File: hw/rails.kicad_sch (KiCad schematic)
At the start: 20 parts, among them U201 LM5164, U202 TLV76733

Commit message: Choose the buck inductor; record three design items the parts exposed
L201: Wurth 7447714330 (WE-PD 1050, 33 uH, Isat 2.9 A typ, AEC-Q200
Grade 1) -- 1.72x the 1.18 A worst peak after a -30% hot derate,
closing the Isat gap buck_preregulator.cir left open. Land pattern is
not in KiCad 7; phase 3.

Three items that are not part choices, each pinned as a check:
- POWER-PATH: injector and EGR current flows through pin 21, the EMI
  filter and a reverse FET sized for 5 A; pins 04/06 are 10 A battery
  feeds used only as senses. L101/L102/F101 wait on the decision.
- BOOST-SLOPE: by TI SLVS861F Eq. 9 the drawn 82 mOhm sense resistor
  exceeds the subharmonic ceiling at cranking (44.9 mOhm), and the
  330 uH it needs does not exist at a 2.2 A saturation rating.
- SENSOR-PTC: real PTCs are specified 0.40-5.00 ohm, not "3.0 ohm
  +/-30%", and Ihold halves at 85 C.

The netlist gate now counts the power ground as an open item: GND
reaches the connector only through sensor-ground pins. Removes a stale
EGR note from the connector sheet.

24/24 sim blocks, netlist gate passing with 2 named open items.
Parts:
- L201: value 33uH -> 7447714330; Chosen (none) -> Wurth WE-PD 1050, 33 uH, Isat 2.9 A typ, IR 2.5 A, 79 mOhm 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; Class (none) -> 33uH; MPN (none) -> 7447714330
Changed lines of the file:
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@@
       (effects (font (size 1.27 1.27)))
     )
-    (property "Value" "33uH" (id 1) (at 284.0 90.08 0)
+    (property "Value" "7447714330" (id 1) (at 284.0 90.08 0)
       (effects (font (size 1.27 1.27)))
     )
@@
       (effects (font (size 1.27 1.27)) hide)
     )
-    (property "Source" "buck_preregulator.cir L1 -- sized by ripple at the 40 V worst case, not at nominal" (id 4) (at 284.0 85.0 0)
+    (property "MPN" "7447714330" (id 4) (at 284.0 85.0 0)
       (effects (font (size 1.27 1.27)) hide)
     )
+    (property "Class" "33uH" (id 5) (at 284.0 85.0 0)
+      (effects (font (size 1.27 1.27)) hide)
+    )
+    (property "Chosen" "Wurth WE-PD 1050, 33 uH, Isat 2.9 A typ, IR 2.5 A, 79 mOhm max, AEC-Q200 Grade 1. No WE-PD land pattern in KiCad 7 -- drawn in phase 3 from the Wurth drawing" (id 6) (at 284.0 85.0 0)
+      (effects (font (size 1.27 1.27)) hide)
+    )
+    (property "Source" "buck_preregulator.cir L1 -- sized by ripple at the 40 V worst case, not at nominal" (id 7) (at 284.0 85.0 0)
+      (effects (font (size 1.27 1.27)) hide)
+    )

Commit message: Package every resistor and capacitor from the voltage across it
hw/assign_passives.py sizes all 188 chip R and C from a per-net table
of continuous and peak voltage (73.3 V pulse 2a, 104 V boost, bootstrap
domains riding on the bank nodes), against Vishay CRCW e3 resistor
ratings (Umax with 1.09x margin, power derated to 0.588x at a 105 C
board) and KEMET's automotive X7R waterfall (parsed by x-coordinate;
the text layout misreads its columns). schlib.place() applies the map
by ref and value; check_netlist fails on any unpackaged R or C.

Found along the way:
- 4.7 uF at 100 V is not in automotive X7R. The EMI filter C1, buck
  input and boost input are now 2 x 2.2 uF 100 V 1210; emi_filter.cir
  models the pair and its cold corner was re-pinned (0.6 dB worse).
- The twelve 470 ohm gate pulldowns need 2010: 0.31 W each at 100%
  duty. Recorded; 1k may now be possible against the real Crss.
- Local labels at 180 degrees were justified in the wrong frame on
  every sheet -- the bug fixed for hierarchical labels earlier -- so
  their text sat across their own wire. Fixed in schlib.label().

Internal nodes whose voltage matters now carry names (FB_BOOST_MID,
CAN1_SPLIT, ...); auto-names like Net-(R407-Pad2) move when parts are
added ahead of them.

24/24 sim blocks, netlist gate passing, 264 of 302 parts footprinted.
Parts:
- added C207: 10uF, Capacitor_SMD:C_0805_2012Metric, symbol Device:C
- C201: value 4.7uF/100V -> 2.2uF 100V; footprint (none) -> Capacitor_SMD:C_1210_3225Metric; Source buck input bypass -- LM5164 datasheet sec.4, 'short, low impedance paths' to VIN -> buck input bypass -- LM5164 datasheet sec.4, 'short, low impedance paths' to VIN; one of two
- C202: value 2.2nF/50V X7R -> 2.2uF 100V; footprint (none) -> Capacitor_SMD:C_1210_3225Metric; Source LM5164 sec.4 pin 7 -- 'a high-quality 2.2nF 50V X7R ceramic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 -> buck input bypass -- LM5164 datasheet sec.4, 'short, low im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
- C203: value 47uF/10mOhm -> 2.2nF/50V X7R; footprint (none) -> Capacitor_SMD:C_0603_1608Metric; Source buck_preregulator.cir C1/Re1 -- 47 uF with 10 mOhm ESR; the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 -> LM5164 sec.4 pin 7 -- 'a high-quality 2.2nF 50V X7R ceramic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
- C204: value 100nF -> 47uF/10mOhm; footprint (none) -> Capacitor_SMD:C_1210_3225Metric; Source high-frequency bypass at the buck output -> buck_preregulator.cir C1/Re1 -- 47 uF with 10 mOhm ESR; the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
- C205: value 1uF -> 100nF; footprint (none) -> Capacitor_SMD:C_0603_1608Metric; Source TLV767 sec.5 -- input capacitor, close to IN and GND -> high-frequency bypass at the buck output
- C206: value 10uF -> 1uF; footprint (none) -> Capacitor_SMD:C_0805_2012Metric; Source TLV767 sec.5 -- output capacitor -> TLV767 sec.5 -- input capacitor, close to IN and GND
- R201: footprint (none) -> Resistor_SMD:R_0805_2012Metric
- R202, R203, R204, R205, R206, R207, R208: footprint (none) -> Resistor_SMD:R_0603_1608Metric
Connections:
- net 3V3_MCU: now also C207.1; no longer C206.1
- net 5V_MAIN: now also C206.1; no longer C203.1
- net BST: now also C203.1; no longer C202.1
- net GND: now also C202.2, C207.2; no longer C203.2
- net SW: now also C203.2; no longer C202.2
- net VBAT_PROT: now also C202.1

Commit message: Build SENSOR-PTC: a tracker per sensor group behind a TPS48110-Q1 cut-off
The three PTCs (F201-F203) are gone. Each sensor group has a
TPS7B4253-Q1 tracking 5V_MAIN to +/-4 mV, so a shorted group limits in
its own regulator and the rest of the board never sees it. The three
share VSNS, fed from VBAT_PROT through an IPD90N10S4-06 switched by a
TPS48110-Q1. It opens above 40.52-42.08 V (340k/10k at 0.1%) and stays
closed through the 40 V load dump. VSNS has 47 uF of hold-up.

sensor_rail.cir is rewritten. It applies pulse 2a through the real
pin-21 filter and runs three corners. The trackers' input peaks at
22.3 V against their 45 V rating, because TI's inrush network (100k /
22 nF) makes the FET a source follower for fast edges; the comparator
opens it as well. VS and CS are fed through 100 ohm + 22 nF, giving
4.9 V/us against their 60 V/us limit. The hold-up is enough aged to
33 uF with every tracker at its limit. An ideal-switch model chattered
on reclose and ngspice could not follow it, so the FET is modelled with
its gate network. Found on the way: with L1 unsaturated, the clamp node
reaches 76.6 V, not 73.3 V; still 100 V class, and now a check.

New symbols for both ICs, drawn from SLVSCP3D and SLUSEE5E. Their land
patterns are still to draw: no KiCad DGX-19, and TI's DDA0008J matches
no KiCad variant. The output capacitors face the harness, so they are
50 V 2220, and assign_passives can now use 2220. The circuit handbook
entry is redrawn and regenerated. Decisions log 4 and 7, BOM
requirements, status and the handoff are updated, and the bible is
rebuilt (357 pages).

Gates: 25/25 blocks, connectivity OK, 353 components, 335 with
footprints, 225 passives.
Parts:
- removed F201, F202, F203: 3.0R 200mA, symbol Device:Polyfuse
- added C208, C209: 22nF, Capacitor_SMD:C_0603_1608Metric, symbol Device:C
- added C210: 1uF, Capacitor_SMD:C_1206_3216Metric, symbol Device:C
- added C211: 47uF 63V, symbol Device:C_Polarized
- added C212, C213, C215, C216, C218, C219: 100nF, Capacitor_SMD:C_0603_1608Metric, symbol Device:C
- added C214, C217, C220: 10uF 50V, Capacitor_SMD:C_2220_5750Metric, symbol Device:C
- added Q201: IPD90N10S4-06, Package_TO_SOT_SMD:TO-252-2, symbol Device:Q_NMOS_GDS
- added R209: 100R, Resistor_SMD:R_0603_1608Metric, symbol Device:R
- added R210: 340k 0.1%, Resistor_SMD:R_0805_2012Metric, symbol Device:R
- added R211: 10k 0.1%, Resistor_SMD:R_0603_1608Metric, symbol Device:R
- added R212: 100k, Resistor_SMD:R_0603_1608Metric, symbol Device:R
- added R213: 10R, Resistor_SMD:R_0603_1608Metric, symbol Device:R
- added U203: TPS48110, symbol ecu25kva:TPS48110
- added U204, U205, U206: TPS7B4253, symbol ecu25kva:TPS7B4253
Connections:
- net 5V_MAIN: now also C213.1, C216.1, C219.1, U203.1 (EN/UVLO), U203.3 (INP), U204.5 (ADJ), U205.5 (ADJ), U206.5 (ADJ)
- net 5V_SENSOR_A: now also C214.1, U204.1 (OUT), U204.4 (FB)
- net 5V_SENSOR_B: now also C217.1, U205.1 (OUT), U205.4 (FB)
- net 5V_SENSOR_C: now also C220.1, U206.1 (OUT), U206.4 (FB)
- net GND: now also C208.2, C211.2, C212.2, C213.2, C214.2, C215.2, C216.2, C217.2, C218.2, C219.2, C220.2, R211.2, R213.2, U203.10 (DIODE), U203.6 (GND), U203.7 (IMON), U203.8 (IWRN), U203.9 (TMR), U204.3 (GND), U204.6 (GND), U204.9 (EP), U205.3 (GND), U205.6 (GND), U205.9 (EP), U206.3 (GND), U206.6 (GND), U206.9 (EP)
- net VBAT_PROT: now also Q201.2 (D), R209.1, R210.1
- new net OVC_BST: C210.1, U203.12 (BST)
- new net OVC_C1R: C209.2, R213.1
- new net OVC_GATE: C209.1, Q201.1 (G), R212.2, U203.14 (PD)
- new net OVC_OV: R210.2, R211.1, U203.2 (OV)
- new net OVC_PU: R212.1, U203.15 (PU)
- new net OVC_VS: C208.1, R209.2, U203.17 (CS-), U203.18 (CS+), U203.19 (ISCP), U203.20 (VS)
- new net VSNS: C210.2, C211.1, C212.1, C215.1, C218.1, Q201.3 (S), U203.13 (SRC), U204.8 (IN), U205.8 (IN), U206.8 (IN)
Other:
- note added: "5V_SENSOR -- TPS48110-Q1 overvoltage cut-off (opens above 40.5-42.1 V, closed through the 40 V dump) feeding one TPS7B4253-Q1 tracker per sensor group. sensor_rail.cir."
- note added: "RATIOMETRIC MONITOR: the divider taps 5V_MAIN, and every sensor group's tracker follows 5V_MAIN to +/-4 mV (0.08%) at any load up to 300 mA. So one tap now corrects all three groups. With the PTCs it could not: each dropped about 150 mV (3%) downstream of the tap."
- note removed: "RATIOMETRIC MONITOR, a limitation worth stating: the divider taps 5V_MAIN, upstream of the PTCs. Each group's own PTC drops about 50 mA x 3.0 ohm = 150 mV, which is 3% of the rail and is NOT captured by a measurement taken before it. Correct for the regulator's drift, not for the protection element's. Moving the tap downstream would fix one group and leave the other two wrong, so the tap stays co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"

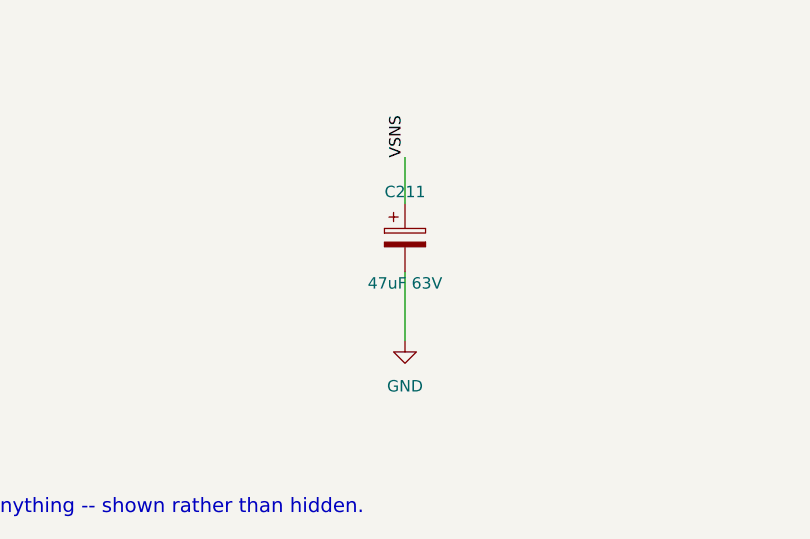
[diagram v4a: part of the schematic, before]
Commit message: Choose the three non-ceramic capacitors; the boost tank becomes a 2-can stack
C313: KEMET T599 150 uF polymer tantalum plus a 22 mOhm series resistor
(R306). No datasheet gives an ESR minimum, so the resistor is PDN-BULK's
floor; the pair is 21.8-72.2 mOhm and mcu_pdn passes both ends at 96 uF.

C211: Chemi-Con HXC 47 uF 63 V hybrid polymer. sensor_rail now runs its
worst corners at 26.3 uF (tolerance plus end of life) and passes.

C401 + C420: two HXC 82 uF 80 V in series, the owner's choice over one
160 V wet can, because no part rated above 100 V publishes a cold ESR.
Worst stack ESR 224 mOhm aged at -55 C; 18 A in 45 us at -40 C. The sims
run 41 uF, every check uses the 85.1 V worst low point, and the 22k bleed
is split 2 x 11k to balance the cans. Decisions log section 9.
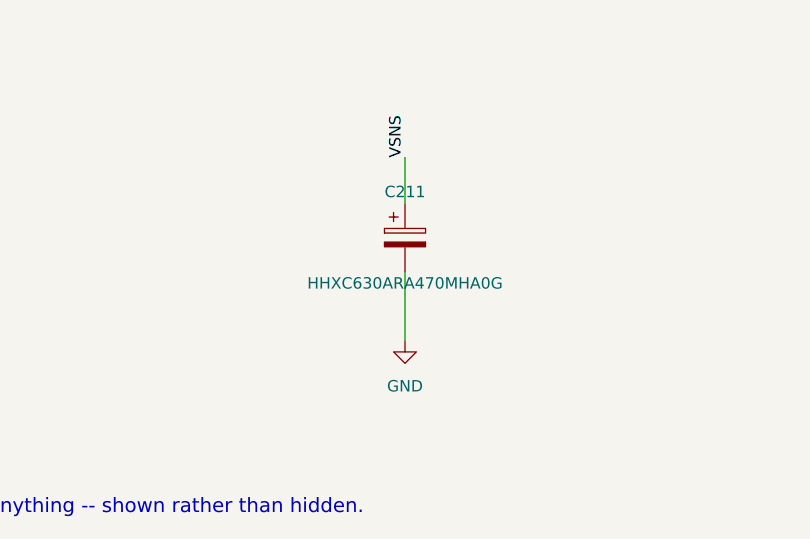
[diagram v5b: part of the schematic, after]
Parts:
- C211: value 47uF 63V -> HHXC630ARA470MHA0G; footprint (none) -> Capacitor_SMD:CP_Elec_8x10; Chosen (none) -> Chemi-Con HXC hybrid polymer, 47 uF, 63 V, 8 x 10 mm, 40 mO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; Class (none) -> 47uF 63V; MPN (none) -> HHXC630ARA470MHA0G
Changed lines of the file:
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@@
       (effects (font (size 1.27 1.27)))
     )
-    (property "Value" "47uF 63V" (id 1) (at 240.0 365.08 0)
+    (property "Value" "HHXC630ARA470MHA0G" (id 1) (at 240.0 365.08 0)
       (effects (font (size 1.27 1.27)))
     )
-    (property "Footprint" "" (id 2) (at 240.0 360.0 0)
+    (property "Footprint" "Capacitor_SMD:CP_Elec_8x10" (id 2) (at 240.0 360.0 0)
       (effects (font (size 1.27 1.27)) hide)
     )
@@
       (effects (font (size 1.27 1.27)) hide)
     )
-    (property "Source" "sensor_rail.cir -- hold-up on VSNS; checked at 33 uF aged" (id 4) (at 240.0 360.0 0)
+    (property "MPN" "HHXC630ARA470MHA0G" (id 4) (at 240.0 360.0 0)
       (effects (font (size 1.27 1.27)) hide)
     )
-    (property "Note" "Not MLCC -- chosen separately, AEC-Q200, 125 C" (id 5) (at 240.0 360.0 0)
+    (property "Class" "47uF 63V" (id 5) (at 240.0 360.0 0)
       (effects (font (size 1.27 1.27)) hide)
     )
+    (property "Chosen" "Chemi-Con HXC hybrid polymer, 47 uF, 63 V, 8 x 10 mm, 40 mOhm max, Z(-55)/Z(20) <= 2 at 100 kHz, 4000 h at 125 C, AEC-Q200" (id 6) (at 240.0 360.0 0)
+      (effects (font (size 1.27 1.27)) hide)
+    )
+    (property "Source" "sensor_rail.cir -- hold-up on VSNS; checked at 33 uF aged" (id 7) (at 240.0 360.0 0)
+      (effects (font (size 1.27 1.27)) hide)
+    )
+    (property "Note" "Not MLCC -- chosen separately, AEC-Q200, 125 C" (id 8) (at 240.0 360.0 0)
+      (effects (font (size 1.27 1.27)) hide)
+    )
